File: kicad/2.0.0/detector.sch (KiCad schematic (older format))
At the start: 44 parts

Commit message: added power leds and test points to 2.0.0
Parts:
- removed C? (x2): 100n, Capacitor_SMD:C_0603_1608Metric, symbol Device:C_Small
- removed C? (x2): 10u, Capacitor_SMD:C_1206_3216Metric, symbol Device:C_Small
- removed C? (x2): 1u, Capacitor_SMD:C_0603_1608Metric, symbol Device:C_Small
- removed D? (x4): D_Small, symbol Device:D_Small
- removed R? (x2): 120, Resistor_SMD:R_0603_1608Metric, symbol Device:R_Small
- removed R? (x2): 1.1k, Resistor_SMD:R_0603_1608Metric, symbol Device:R_Small
- removed U?: LM337, Package_TO_SOT_SMD:SOT-223-3_TabPin2, symbol Regulator_Linear:LM337_SOT223
- removed U?: LM317, Package_TO_SOT_SMD:SOT-223-3_TabPin2, symbol Regulator_Linear:LM317_3PinPackage
- added C? (x2): 1u, Capacitor_SMD:C_0603_1608Metric, symbol Device:C_Small
- added C? (x2): 10u, Capacitor_SMD:C_1206_3216Metric, symbol Device:C_Small
- added C? (x2): 100n, Capacitor_SMD:C_0603_1608Metric, symbol Device:C_Small
- added D? (x2): LED, symbol Device:LED
- added D? (x4): D_Small, symbol Device:D_Small
- added R?: 470, symbol Device:R_Small
- added R?: 510, symbol Device:R_Small
- added R? (x2): 120, Resistor_SMD:R_0603_1608Metric, symbol Device:R_Small
- added R? (x2): 1.1k, Resistor_SMD:R_0603_1608Metric, symbol Device:R_Small
- added TP?: -15V, symbol Connector:TestPoint
- added TP? (x4): +12V, symbol Connector:TestPoint
- added TP? (x3): -12V, symbol Connector:TestPoint
- added TP?: +15V, symbol Connector:TestPoint
- added TP? (x2): GND, symbol Connector:TestPoint
- added TP?: +10V, symbol Connector:TestPoint
- added TP?: BIAS, symbol Connector:TestPoint
- added TP?: -Y1-, symbol Connector:TestPoint
- added TP?: -Y1+, symbol Connector:TestPoint
- added TP?: X2-, symbol Connector:TestPoint
- added TP?: X2+, symbol Connector:TestPoint
- added TP?: -Y1, symbol Connector:TestPoint
- added TP?: -X2, symbol Connector:TestPoint
- added TP?: -X1+, symbol Connector:TestPoint
- added TP?: -Y2+, symbol Connector:TestPoint
- added TP?: -X1, symbol Connector:TestPoint
- added TP?: -Y2, symbol Connector:TestPoint
- added TP?: -X1-, symbol Connector:TestPoint
- added TP?: -Y2-, symbol Connector:TestPoint
- added U?: LM317, Package_TO_SOT_SMD:SOT-223-3_TabPin2, symbol Regulator_Linear:LM317_3PinPackage
- added U?: LM337, Package_TO_SOT_SMD:SOT-223-3_TabPin2, symbol Regulator_Linear:LM337_SOT223
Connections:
- wire segments 148 -> 196
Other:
- note added: "Forward voltages for LEDs:\nRed Vf = 1.8 V, Blue Vf = 3.1 V"
- note added: "POWER INPUT"
- note added: "POWER LEDS"
- note added: "R = (Vs - Vf) / I"
- note added: "SIGNAL OUTPUT"
- note added: "TRANSIMPEDANCE AMPLIFIERS"
- note removed: "DETECTOR AND TRANSIMPEDANCE AMPLIFIERS"
- moved on the sheet: C?, D?A, D?B, D?C, D?D, D?E, R?, U?

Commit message: replaced OPAx197s with standard library symbols, increased voltage regulator caps
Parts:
- removed C? (x2): 18p, Capacitor_SMD:C_0603_1608Metric, symbol Device:C_Small
- removed C? (x4): 100n, Capacitor_SMD:C_0603_1608Metric, symbol Device:C_Small
- removed C? (x2): 1u, Capacitor_SMD:C_0603_1608Metric, symbol Device:C_Small
- removed C? (x2): 10u, Capacitor_SMD:C_1206_3216Metric, symbol Device:C_Small
- removed D? (x2): S599x, Sensor_Optical_Position:S5990, symbol Sensor_Optical_Position:S599x
- removed D? (x4): D_Small, symbol Device:D_Small
- removed R? (x2): 6k, Resistor_SMD:R_0603_1608Metric, symbol Device:R_Small
- removed R? (x2): 120, Resistor_SMD:R_0603_1608Metric, symbol Device:R_Small
- removed R? (x2): 1.1k, Resistor_SMD:R_0603_1608Metric, symbol Device:R_Small
- removed TP?: -15V, symbol Connector:TestPoint
- removed TP? (x3): +12V, symbol Connector:TestPoint
- removed TP? (x3): -12V, symbol Connector:TestPoint
- removed TP?: +15V, symbol Connector:TestPoint
- removed TP?: GND, symbol Connector:TestPoint
- removed TP?: -Y1-, symbol Connector:TestPoint
- removed TP?: -Y1+, symbol Connector:TestPoint
- removed TP?: X2-, symbol Connector:TestPoint
- removed TP?: X2+, symbol Connector:TestPoint
- removed TP?: -Y1, symbol Connector:TestPoint
- removed TP?: -X2, symbol Connector:TestPoint
- removed TP?: -X1+, symbol Connector:TestPoint
- removed TP?: -X1, symbol Connector:TestPoint
- removed TP?: -Y2, symbol Connector:TestPoint
- removed TP?: -X1-, symbol Connector:TestPoint
- removed U? (x6): OPA2197IDR, Package_SO:SOIC-8_3.9x4.9mm_P1.27mm, symbol Amplifier_Operational:OPA2197IDR
- removed U?: LM317, Package_TO_SOT_SMD:SOT-223-3_TabPin2, symbol Regulator_Linear:LM317_3PinPackage
- removed U?: LM337, Package_TO_SOT_SMD:SOT-223-3_TabPin2, symbol Regulator_Linear:LM337_SOT223
- added C? (x2): 18p, Capacitor_SMD:C_0603_1608Metric, symbol Device:C_Small
- added C? (x4): 100n, Capacitor_SMD:C_0603_1608Metric, symbol Device:C_Small
- added C? (x2): 22u, Capacitor_SMD:C_0603_1608Metric, symbol Device:C_Small
- added C? (x2): 10u, Capacitor_SMD:C_1206_3216Metric, symbol Device:C_Small
- added D? (x2): S599x, Sensor_Optical_Position:S5990, symbol Sensor_Optical_Position:S599x
- added D? (x4): D_Small, symbol Device:D_Small
- added R? (x2): 6k, Resistor_SMD:R_0603_1608Metric, symbol Device:R_Small
- added R? (x2): 240, Resistor_SMD:R_0603_1608Metric, symbol Device:R_Small
- added R? (x2): 2.2k, Resistor_SMD:R_0603_1608Metric, symbol Device:R_Small
- added TP? (x3): +12V, symbol Connector:TestPoint
- added TP? (x3): -12V, symbol Connector:TestPoint
- added TP?: -X1+, symbol Connector:TestPoint
- added TP?: -X1-, symbol Connector:TestPoint
- added TP?: -X1, symbol Connector:TestPoint
- added TP?: -Y2, symbol Connector:TestPoint
- added TP?: -X2+, symbol Connector:TestPoint
- added TP?: -X2-, symbol Connector:TestPoint
- added TP?: -Y1+, symbol Connector:TestPoint
- added TP?: -Y1-, symbol Connector:TestPoint
- added TP?: -Y1, symbol Connector:TestPoint
- added TP?: -X2, symbol Connector:TestPoint
- added TP?: -15V, symbol Connector:TestPoint
- added TP?: +15V, symbol Connector:TestPoint
- added TP?: GND, symbol Connector:TestPoint
- added U? (x6): OPA2197xD, Package_SO:SOIC-8_3.9x4.9mm_P1.27mm, symbol Amplifier_Operational:OPA2197xD
- added U?: LM317, Package_TO_SOT_SMD:SOT-223-3_TabPin2, symbol Regulator_Linear:LM317_3PinPackage
- added U?: LM337, Package_TO_SOT_SMD:SOT-223-3_TabPin2, symbol Regulator_Linear:LM337_SOT223
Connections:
- wire segments 196 -> 194
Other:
- note added: "Vout = 1.25 V * (1 + 2200 / 240) = 12.7 V"
- note removed: "Vout = 1.25 V * (1 + R / 120) = 12.7 V"
- moved on the sheet: C?, D?A, D?D, R?, TP?

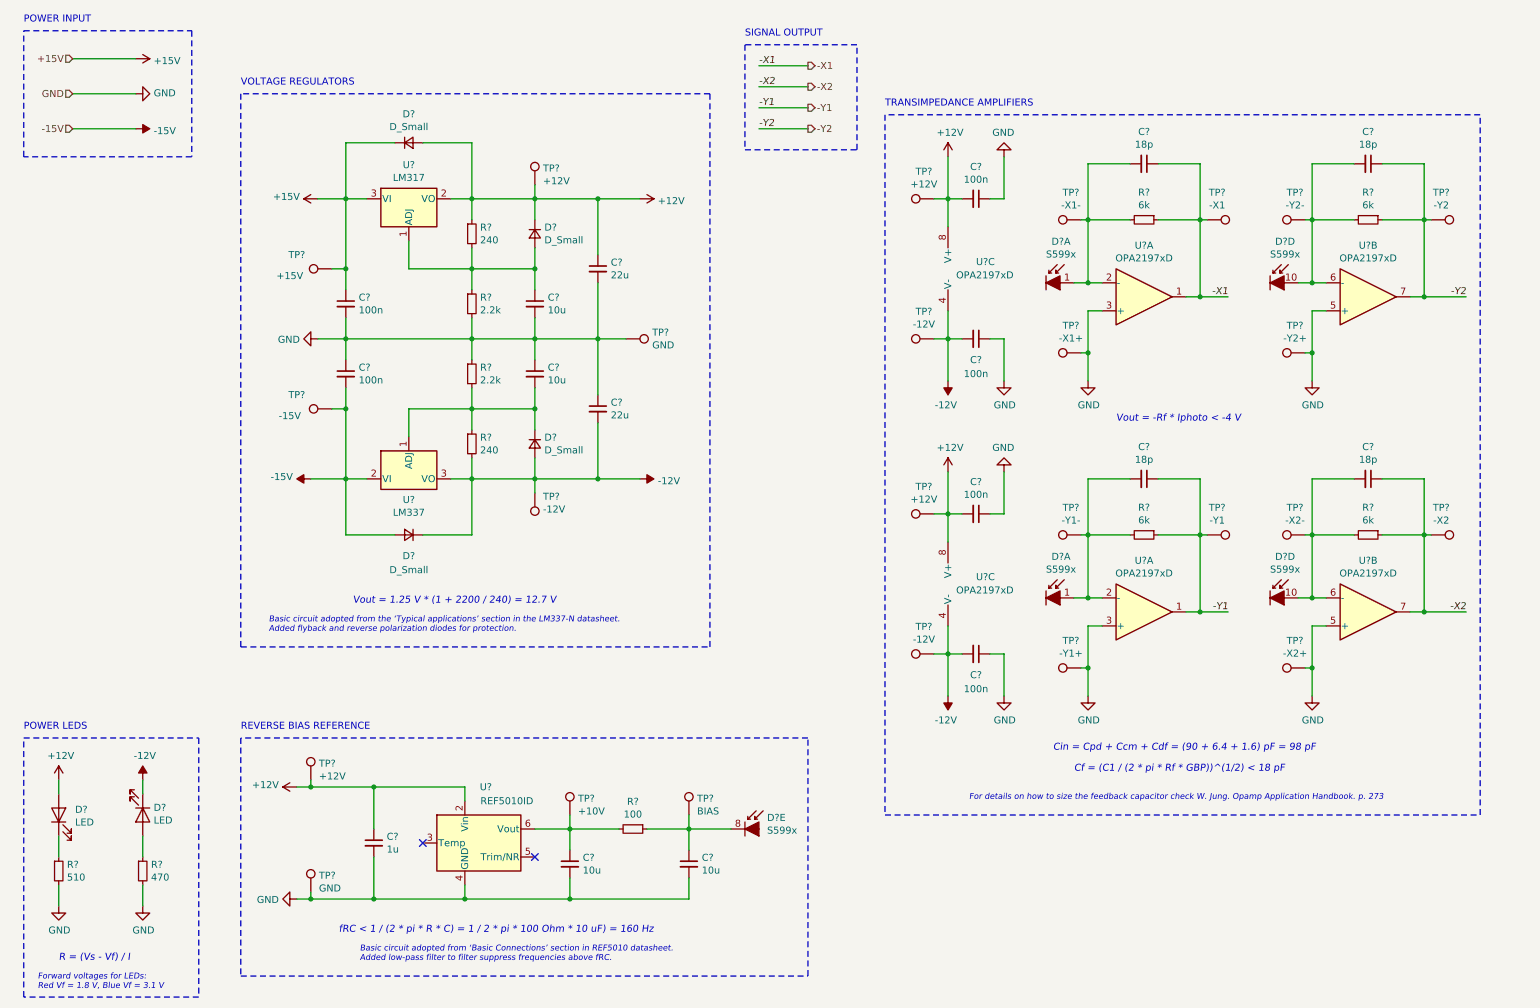
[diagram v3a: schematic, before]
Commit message: created extra projects for arithmetic and detector sheet
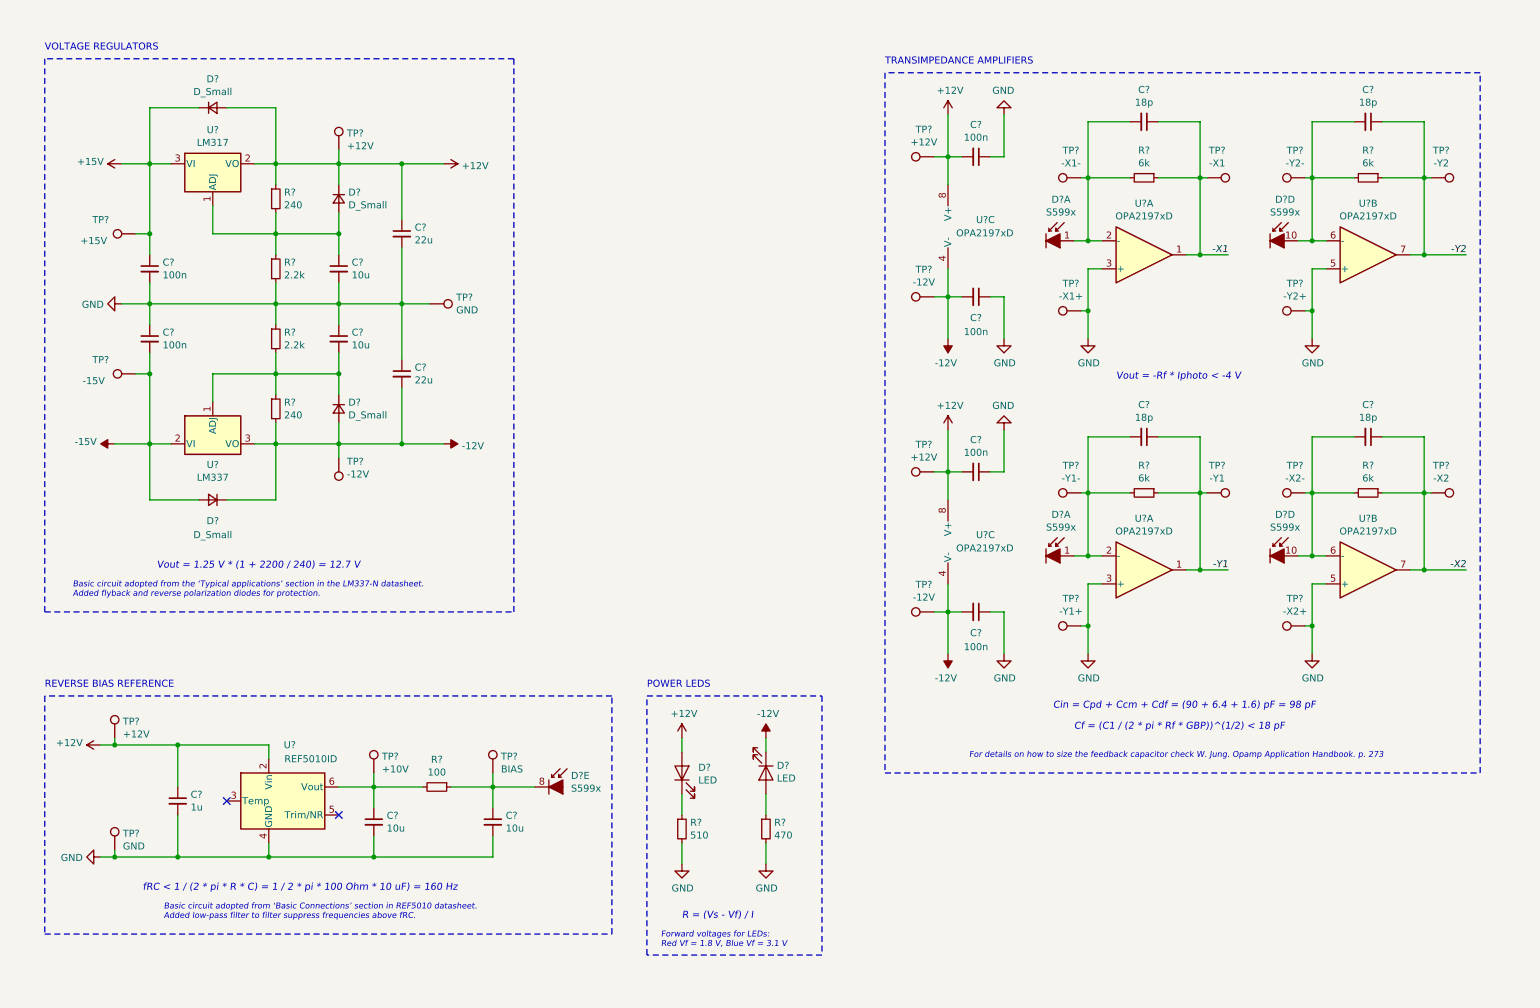
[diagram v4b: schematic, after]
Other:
- note removed: "POWER INPUT"
- note removed: "SIGNAL OUTPUT"
- moved on the sheet: C?, D?, D?A, D?D, D?E, R?, TP?, U?, U?A, U?B, U?C

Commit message: assigned footprints to detector schema, created detector pcb file
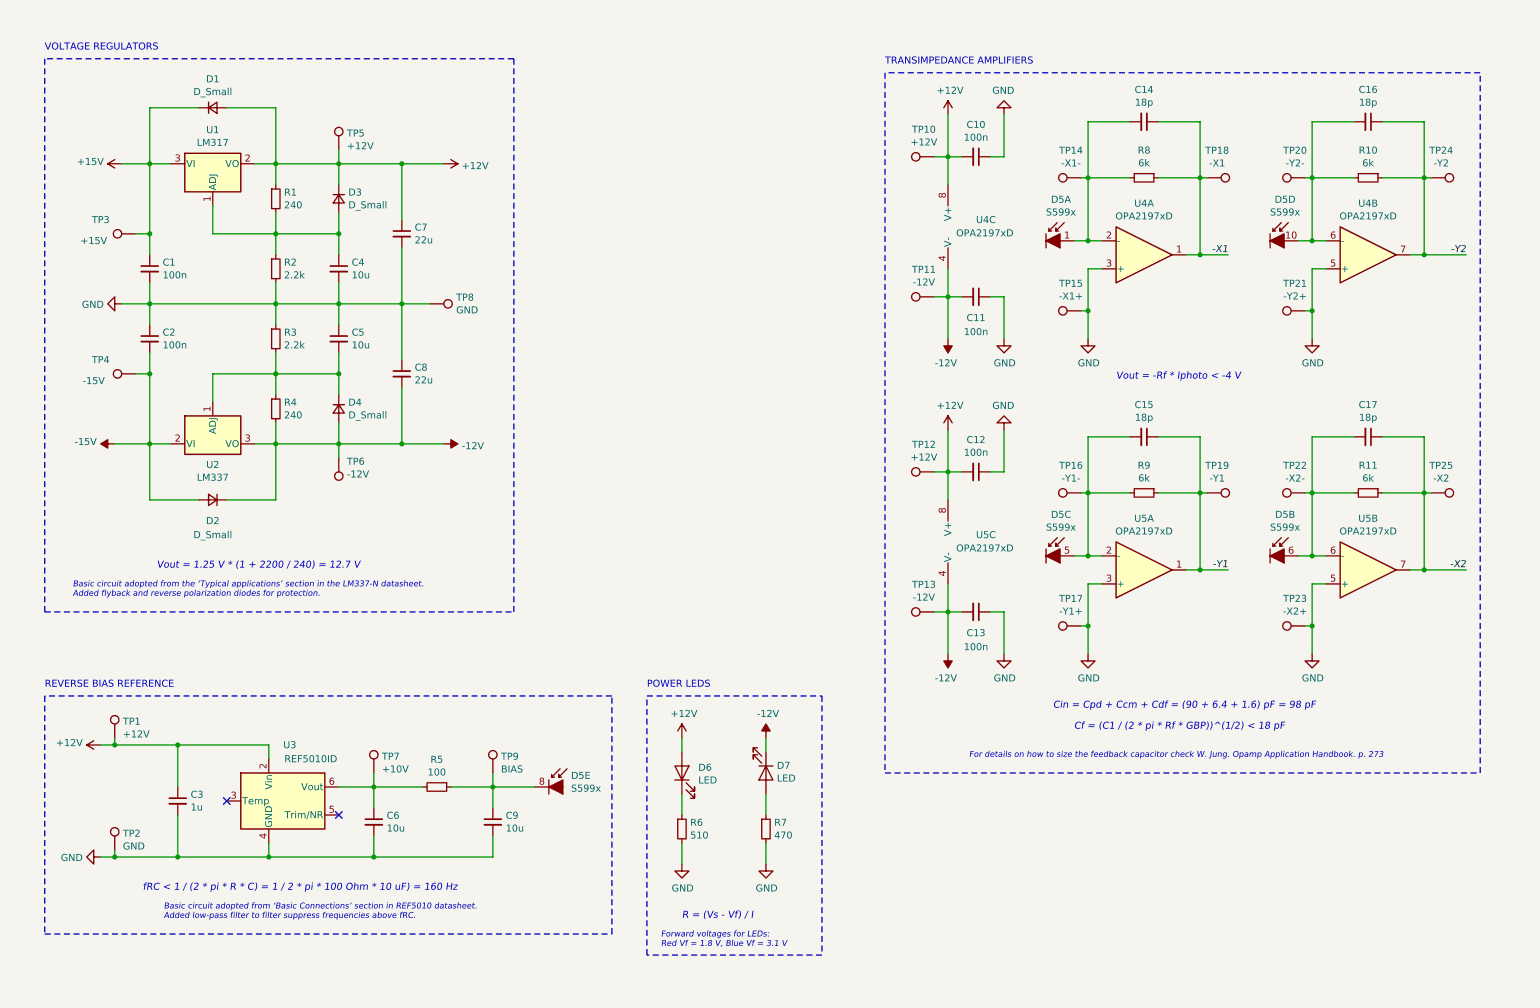
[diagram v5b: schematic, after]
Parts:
- removed D? (x2): S599x, Sensor_Optical_Position:S5990, symbol Sensor_Optical_Position:S599x
- added unit 2 of D5
- added unit 3 of D5
- C3: renamed from C?; footprint (none) -> Capacitor_SMD:C_0603_1608Metric
- C6, C9: renamed from C?; footprint (none) -> Capacitor_SMD:C_1206_3216Metric
- C7, C8: renamed from C?; footprint Capacitor_SMD:C_0603_1608Metric -> Capacitor_SMD:C_1206_3216Metric
- D1, D2, D3, D4: renamed from D?; footprint (none) -> Diode_SMD:D_SOD-123
- D6, D7: renamed from D?; footprint (none) -> Diode_SMD:D_0805_2012Metric
- R5, R6, R7: renamed from R?; footprint (none) -> Resistor_SMD:R_0603_1608Metric
- TP1, TP10, TP11, TP12, TP13, TP14, TP15, TP16, TP17, TP18, TP19, TP2, TP20, TP21, TP22, TP23, TP24, TP25, TP3, TP4, TP5, TP6, TP7, TP8, TP9: renamed from TP?; footprint (none) -> TestPoint:TestPoint_Pad_D1.0mm
- gave numbers to parts that had none: 26
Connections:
- net at C17.2, R11.2, TP22.1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: now also D5.6 (Anode_X2)
- net at C15.2, R9.2, TP16.1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: now also D5.5 (Anode_Y1)
